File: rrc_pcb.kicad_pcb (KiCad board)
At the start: 2 copper layers, 130 x 55 mm, 10 parts, among them J1 Voltage Regulator Input, U1 ADXL357Z, U2 Teensy3.6-teensy, U3 BN220-GPS, U4 MS5611

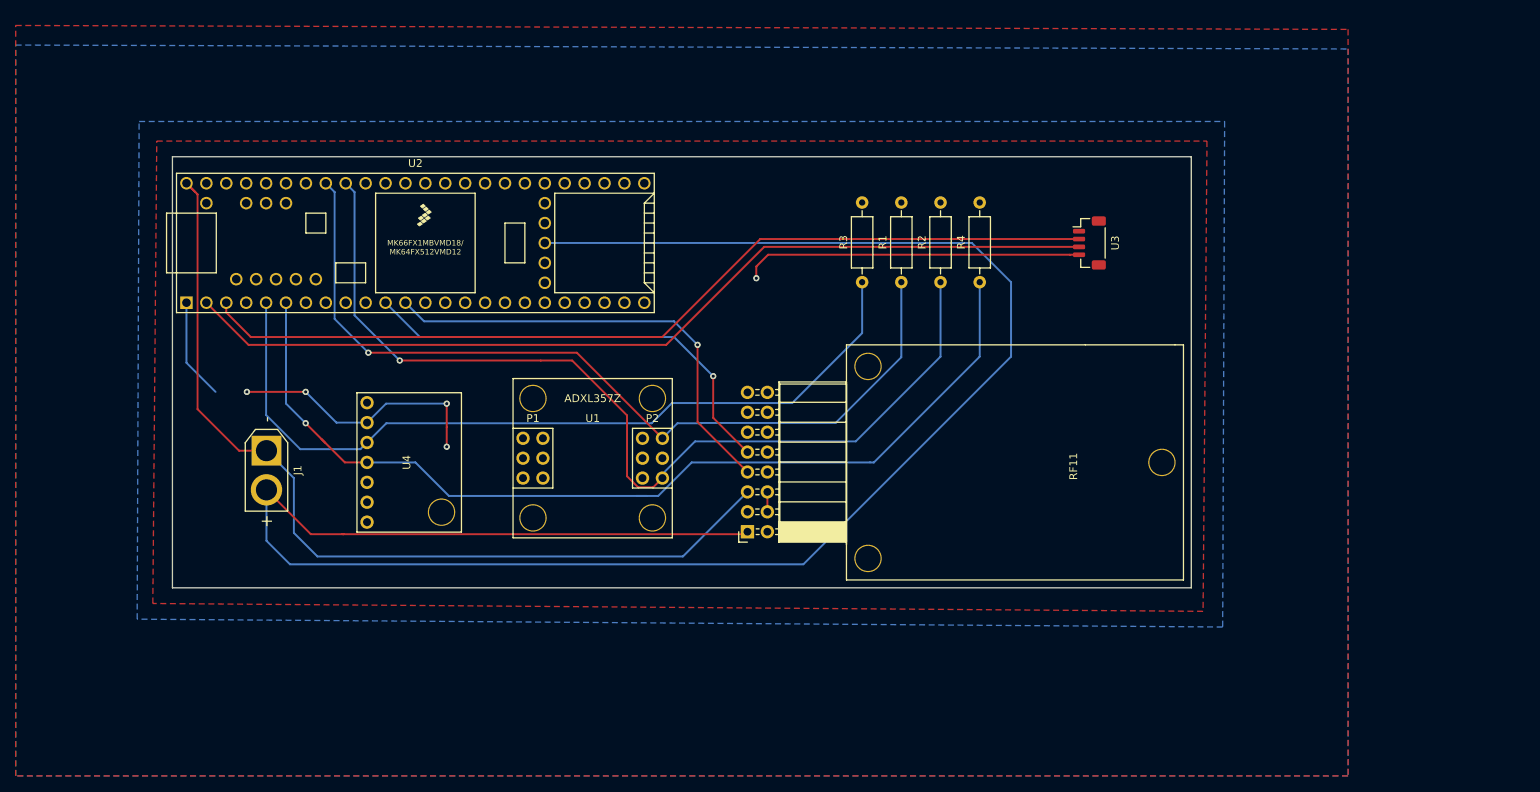
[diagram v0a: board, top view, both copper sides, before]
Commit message: added mounting holes
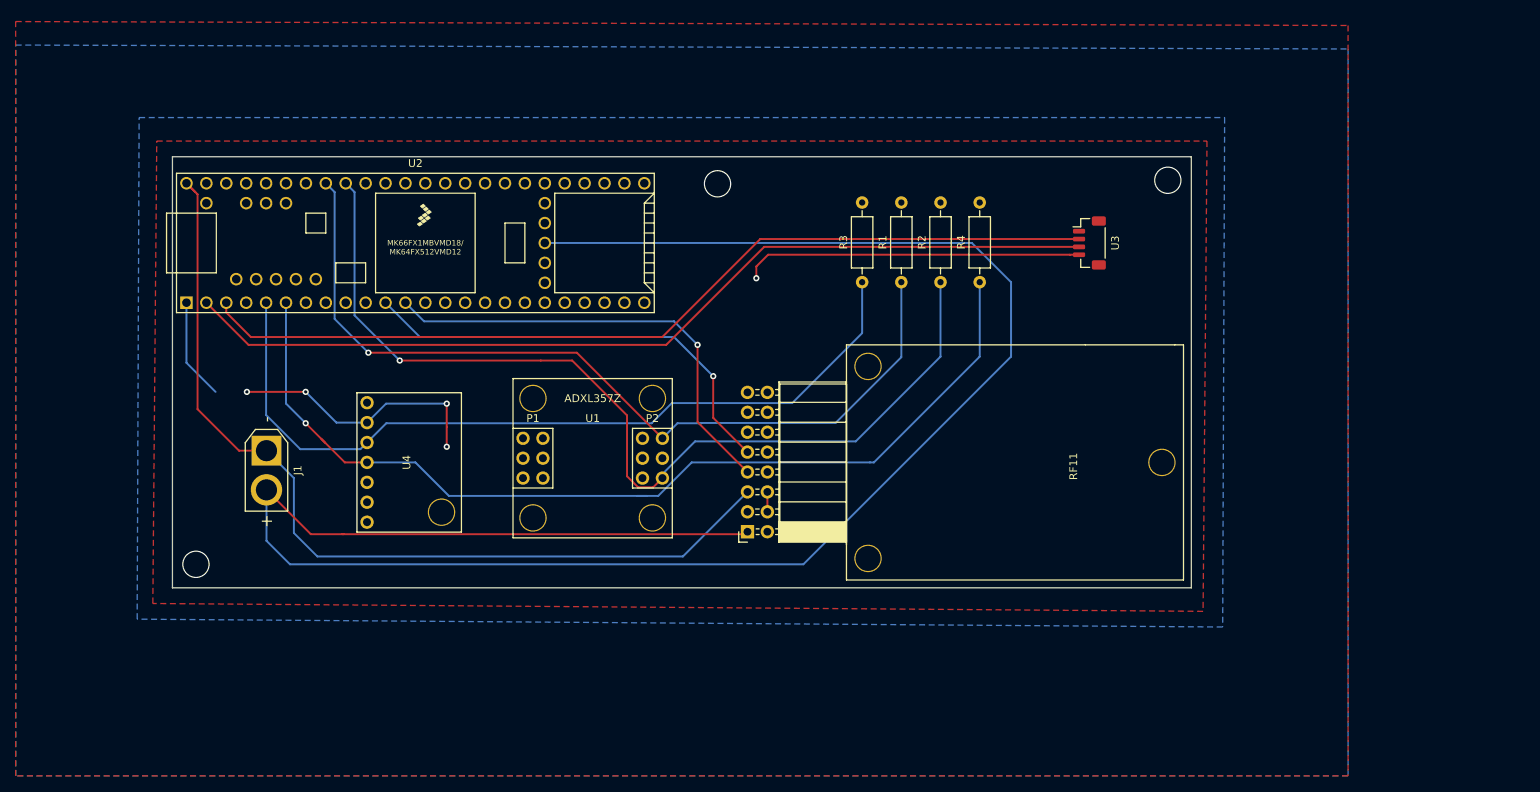
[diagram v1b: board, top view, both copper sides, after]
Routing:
- net T_GND: vias 5 -> 8

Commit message: new pcb layout
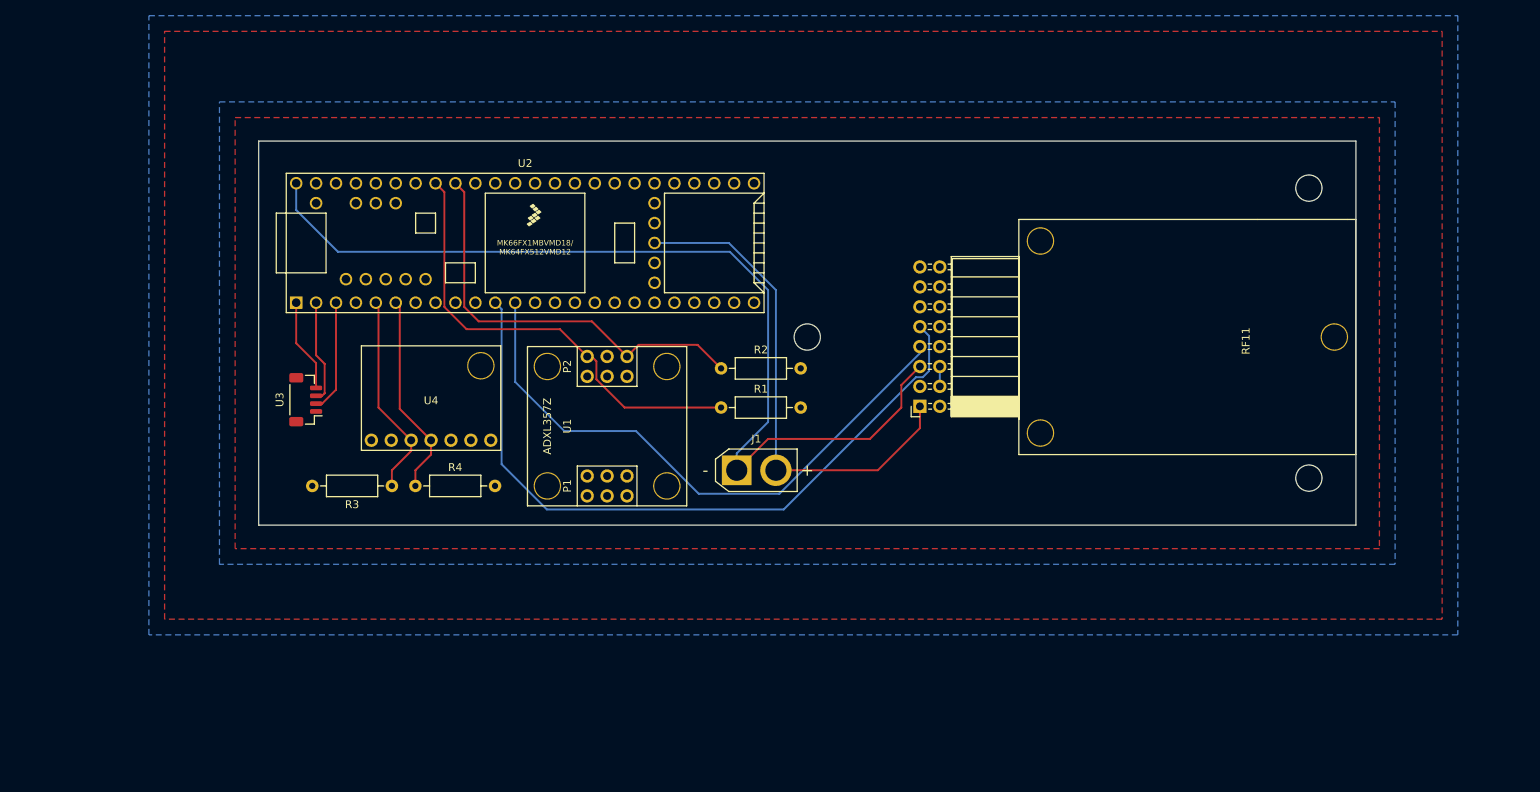
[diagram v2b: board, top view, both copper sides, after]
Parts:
- moved U3 102.0 mm to (62.0, 111.0), turned to 90 degrees
- moved R4 76.6 mm to (76.0, 122.0), turned to 0 degrees
- moved R3 65.4 mm to (73.0, 122.0), turned to 180 degrees
- moved J1 60.1 mm to (117.0, 120.0), turned to 0 degrees
- moved R2 30.1 mm to (115.0, 107.0), turned to 0 degrees
- moved R1 28.0 mm to (115.0, 112.0), turned to 0 degrees
- moved RF11 27.2 mm to (153.0, 88.0)
- moved U2 14.0 mm to (90.0, 91.0)
- moved U1 12.0 mm to (103.0, 122.0), turned to 90 degrees
- moved U4 12.0 mm to (78.0, 120.0), turned to 0 degrees
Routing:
- net GND: track 248.8 -> 64.4 mm
- net Net-(U2-Pad2): track 118.8 -> 13.2 mm
- net Net-(U2-Pad3): track 116.5 -> 14.4 mm
- net Net-(R4-Pad1): track 125.1 -> 26.1 mm, vias 1 -> 0
- net Net-(R3-Pad1): track 104.8 -> 26.3 mm
- net T_GND: track 89.8 -> 11.9 mm, vias 8 -> 0
- net Net-(R2-Pad1): track 122.4 -> 53.5 mm, vias 1 -> 0
- net Net-(R1-Pad1): track 110.8 -> 58.2 mm, vias 1 -> 0
- net Net-(RF11-Pad9): track 57.2 -> 91.3 mm, vias 1 -> 0
- net Net-(RF11-Pad7): track 58.4 -> 75.9 mm, vias 1 -> 0
- net VCC: track 116.5 -> 123.0 mm
- net (no net): vias 0 -> 3
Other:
- board size 130 x 55 mm -> 140 x 49 mm

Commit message: edit
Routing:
- net T_GND: track 11.9 -> 36.3 mm, vias 0 -> 3
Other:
- board size 140 x 49 mm -> 139 x 49 mm

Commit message: AC_added cool RRC logo
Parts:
- added RRC logo: logo, logo:RRC_logo, B.Cu at (171.4, 100.3)

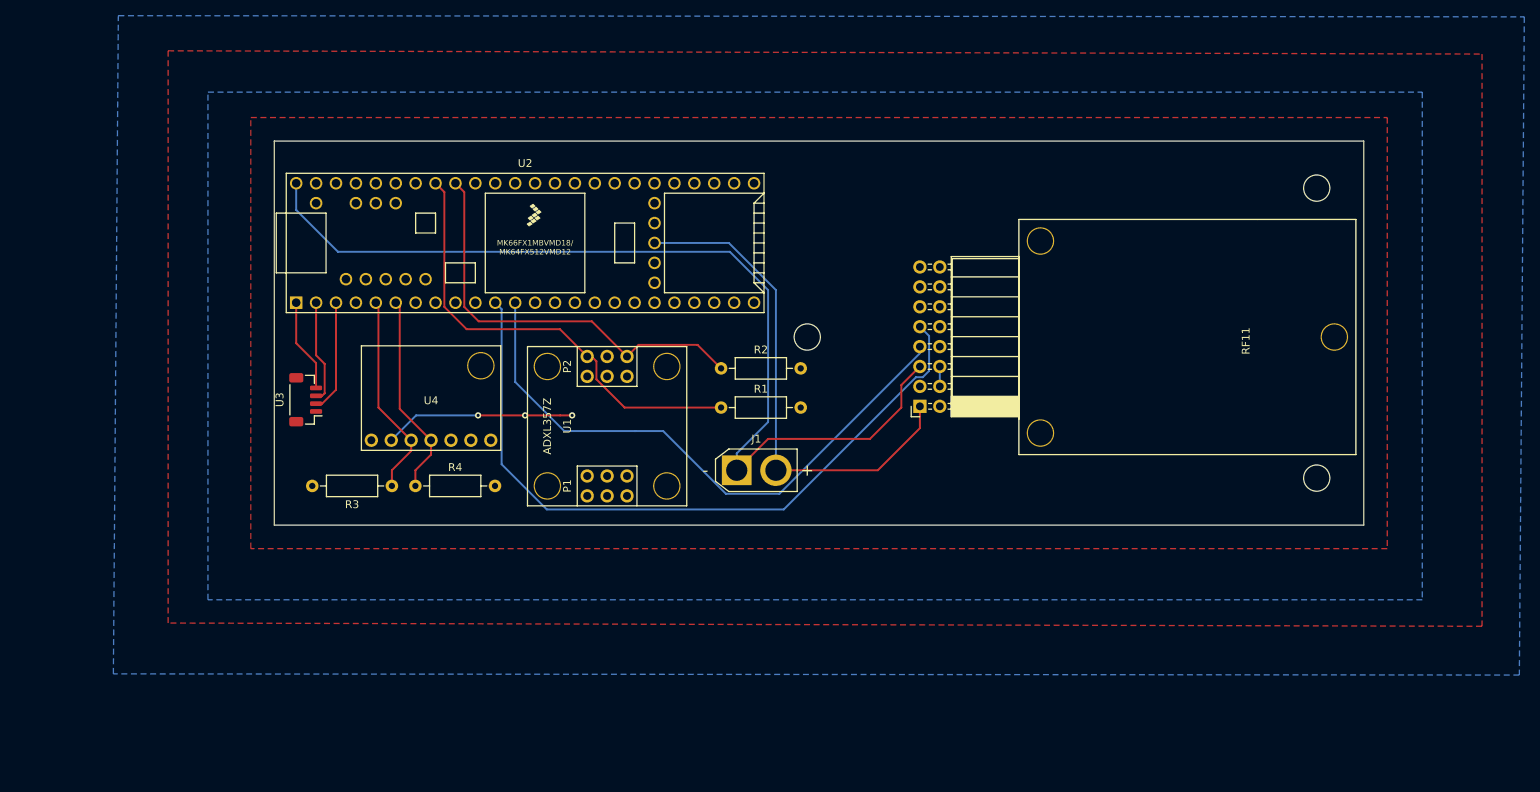
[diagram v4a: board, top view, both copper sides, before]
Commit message: added buzzer
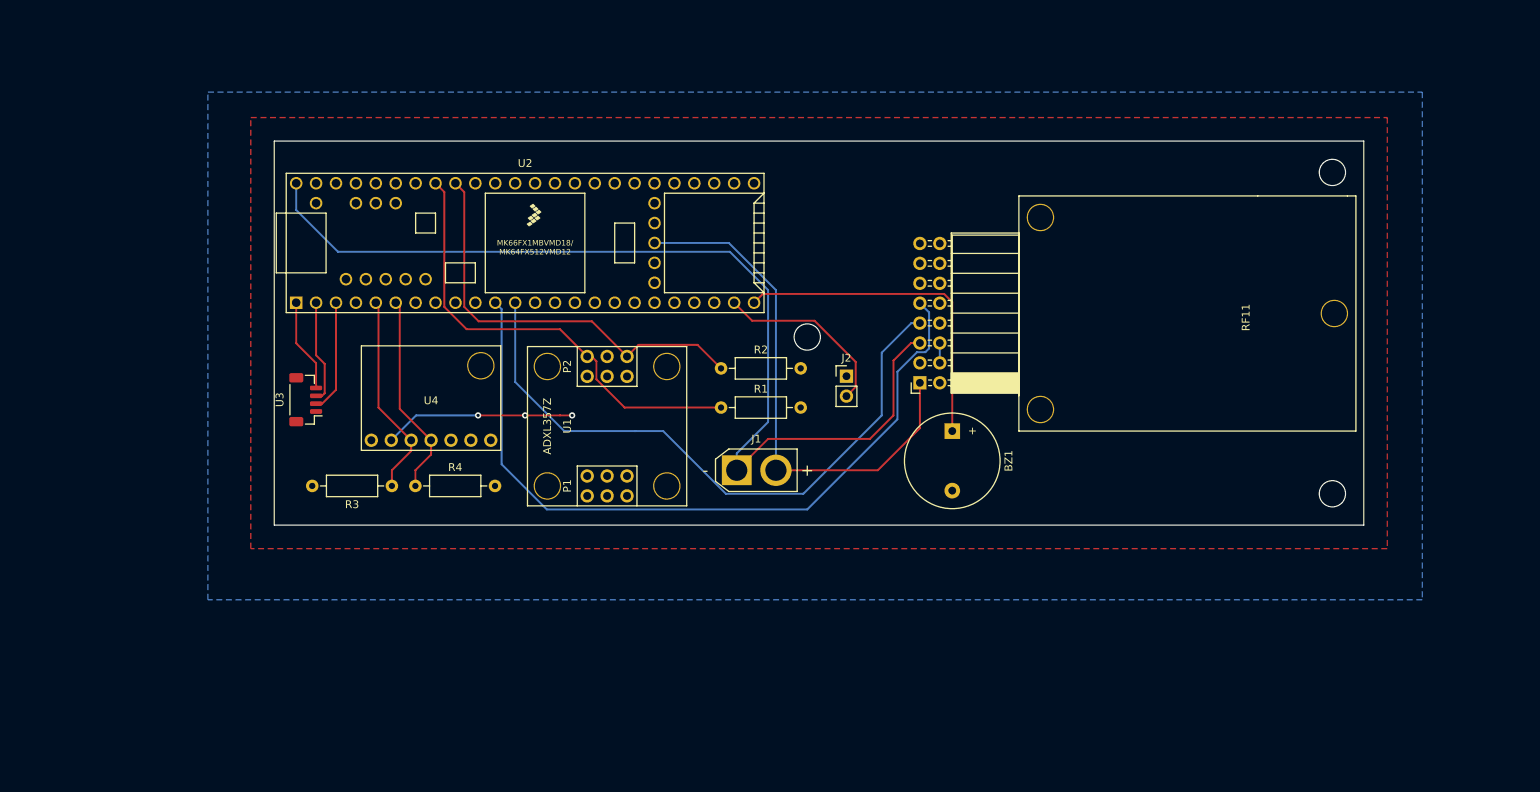
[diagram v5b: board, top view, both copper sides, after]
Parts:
- removed RRC logo: logo, logo:RRC_logo
- added BZ1: Buzzer, Buzzer_Beeper:Buzzer_12x9.5RM7.6, F.Cu at (144.5, 115.0)
- added J2: Conn_01x02_Male, Connector_PinHeader_2.54mm:PinHeader_1x02_P2.54mm_Vertical, F.Cu at (131.0, 108.0)
- added U5: logo, logo:RRC_logo, B.Cu at (171.5, 102.5)
- moved RF11 3.00 mm to (153.0, 85.0)
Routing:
- net Net-(BZ1-Pad1): track 0.00 -> 42.6 mm
- net Net-(J2-Pad2): track 0.00 -> 23.5 mm
- net Net-(RF11-Pad7): track 76.1 -> 81.5 mm
- net Net-(RF11-Pad9): track 91.3 -> 96.2 mm
- net GND: track 64.4 -> 68.2 mm
- net VCC: track 123.0 -> 126.7 mm
- removed copper zone on B.Cu, net (none)
- removed copper zone on F.Cu, net (none)

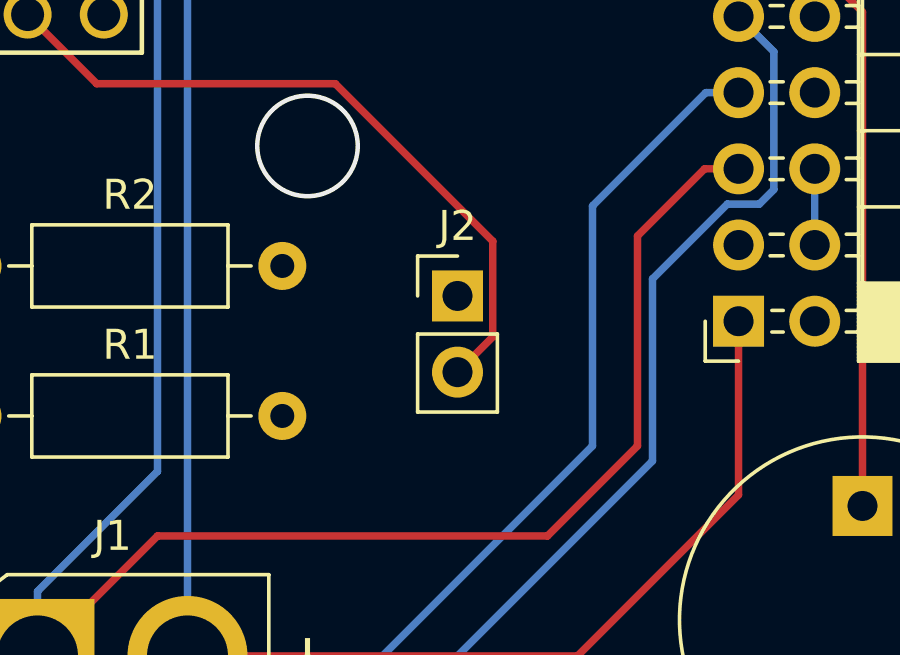
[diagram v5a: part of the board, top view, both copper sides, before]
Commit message: added buzzer enable pin
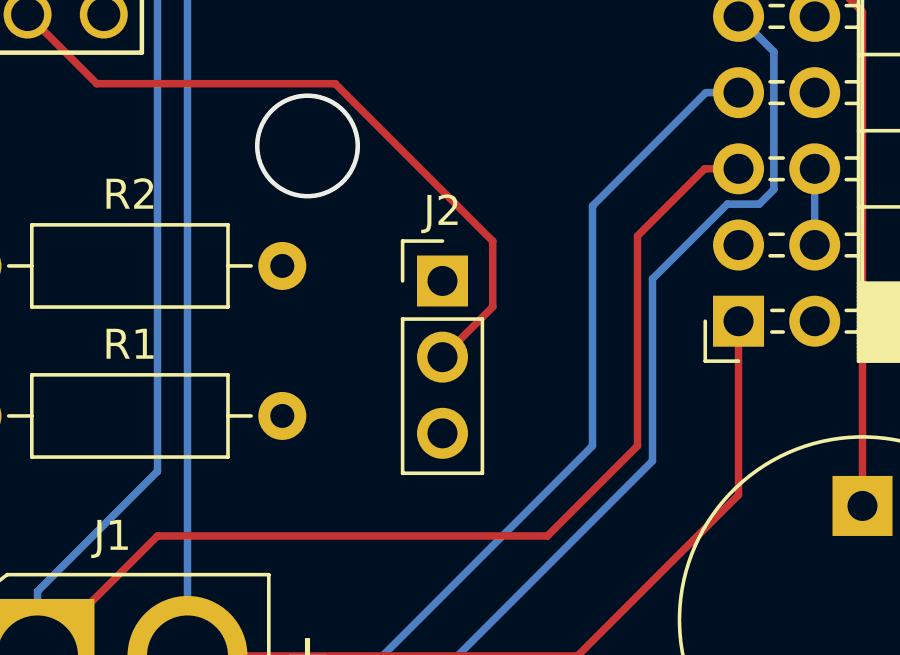
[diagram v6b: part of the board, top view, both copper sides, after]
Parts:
- J2: value Conn_01x02_Male -> Conn_01x03_Male; footprint Connector_PinHeader_2.54mm:PinHeader_1x02_P2.54mm_Vertical -> Connector_PinHeader_2.54mm:PinHeader_1x03_P2.54mm_Vertical
- moved J2 0.71 mm to (130.5, 107.5)
